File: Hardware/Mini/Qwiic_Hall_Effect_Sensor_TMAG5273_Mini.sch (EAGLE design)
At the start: 30 parts, among them J1 Vertical Qwiic Connector, J2 Vertical Qwiic Connector, Q1 20V/4.2A/52mΩ/1.4W, U1 TMAG5273

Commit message: Design Review Changes
Adjusted schematic to have the correct power-on reset circuit, along with the change in the layout. The GPIO net was relabled to RESET to match the layout of the board/labeling. Adjusted some labeling in the schematic.
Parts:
- removed R1: 330, SparkFun-Resistors:330OHM-0603-1/10W-1%
- removed R6: 10k, SparkFun-Resistors:10KOHM-0603-1/10W-1%
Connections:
- net INT renamed !INT
- removed net GPIO: J3.5, R6.1, R7.1
- removed net N$7: Q1.G, R6.2
- new net RESET: J3.5, Q1.G, R7.2
- net 3.3V: now also Q1.S; no longer R1.2, R7.2
- net 3.3V_SW: now also Q1.D; no longer Q1.S, R1.1
- net GND: now also R7.1; no longer Q1.D
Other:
- note added: "7-bit unshifted I2C Address: 0x35"
- note removed: "7-bit unshifted I2C Address: 0x35h"
- moved on the sheet: Q1, R7

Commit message: Adjusted from design review
Added truth tables, changed RESET to Disable, adjusted magnetic axis to be centered to the middle of the board, added push button for 1x1 reset option
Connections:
- net RESET renamed DISABLE
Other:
- note added: "Board Status"
- note added: "DISABLE Value"
- note added: "Disable to Header Reset"
- note added: "HIGH (3.3V)"
- note added: "LOW (0V) - default"
- note added: "Off"
- note added: "On"
- moved on the sheet: Q1, R7
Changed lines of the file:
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@@
 <wire x1="147.32" y1="35.56" x2="147.32" y2="114.3" width="0.2032" layer="97" style="longdash"/>
 <wire x1="195.58" y1="114.3" x2="195.58" y2="35.56" width="0.2032" layer="97" style="longdash"/>
+<wire x1="30.48" y1="121.92" x2="48.26" y2="121.92" width="0.2032" layer="97"/>
+<wire x1="48.26" y1="121.92" x2="60.96" y2="121.92" width="0.2032" layer="97"/>
+<wire x1="60.96" y1="121.92" x2="60.96" y2="129.54" width="0.2032" layer="97"/>
+<wire x1="60.96" y1="129.54" x2="48.26" y2="129.54" width="0.2032" layer="97"/>
+<wire x1="48.26" y1="129.54" x2="30.48" y2="129.54" width="0.2032" layer="97"/>
+<wire x1="48.26" y1="129.54" x2="48.26" y2="121.92" width="0.2032" layer="97"/>
+<text x="31.242" y="130.302" size="1.27" layer="97" font="vector">Disable to Header Reset</text>
+<wire x1="30.48" y1="129.54" x2="30.48" y2="121.92" width="0.2032" layer="97"/>
+<wire x1="30.48" y1="127" x2="60.96" y2="127" width="0.2032" layer="97"/>
+<wire x1="30.48" y1="124.46" x2="60.96" y2="124.46" width="0.2032" layer="97"/>
+<text x="33.02" y="127.508" size="1.27" layer="97" font="vector">DISABLE Value</text>
+<text x="30.988" y="124.968" size="1.27" layer="97" font="vector">HIGH (3.3V)</text>
+<text x="30.988" y="122.428" size="1.27" layer="97" font="vector">LOW (0V) - default</text>
+<text x="48.768" y="124.968" size="1.27" layer="97" font="vector">Off</text>
+<text x="48.768" y="122.428" size="1.27" layer="97" font="vector">On</text>
+<text x="49.276" y="127.508" size="1.27" layer="97" font="vector">Board Status</text>
 </plain>
 <instances>
@@
 <attribute name="VALUE" x="174.244" y="81.28" size="1.778" layer="96" font="vector" rot="R90" align="top-center"/>
 </instance>
-<instance part="SUPPLY8" gate="G$1" x="50.8" y="160.02" smashed="yes">
-<attribute name="VALUE" x="50.8" y="162.814" size="1.778" layer="96" font="vector" align="bottom-center"/>
-</instance>
-<instance part="Q1" gate="G$1" x="48.26" y="152.4" smashed="yes" rot="MR180">
-<attribute name="NAME" x="53.34" y="154.94" size="1.778" layer="95" font="vector" rot="MR180"/>
-<attribute name="VALUE" x="53.34" y="157.48" size="1.778" layer="96" font="vector" rot="MR180"/>
-</instance>
-<instance part="SUPPLY11" gate="G$1" x="58.42" y="144.78" smashed="yes">
-<attribute name="VALUE" x="58.42" y="147.574" size="1.778" layer="96" font="vector" align="bottom-center"/>
-</instance>
-<instance part="R7" gate="G$1" x="38.1" y="147.32" smashed="yes" rot="R90">
-<attribute name="NAME" x="36.576" y="147.32" size="1.778" layer="95" font="vector" rot="R90" align="bottom-center"/>
-<attribute name="VALUE" x="39.624" y="147.32" size="1.778" layer="96" font="vector" rot="R90" align="top-center"/>
-</instance>
-<instance part="GND7" gate="1" x="38.1" y="137.16" smashed="yes">
-<attribute name="VALUE" x="38.1" y="136.906" size="1.778" layer="96" font="vector" align="top-center"/>
+<instance part="SUPPLY8" gate="G$1" x="50.8" y="165.1" smashed="yes">
+<attribute name="VALUE" x="50.8" y="167.894" size="1.778" layer="96" font="vector" align="bottom-center"/>
+</instance>
+<instance part="Q1" gate="G$1" x="48.26" y="157.48" smashed="yes" rot="MR180">
+<attribute name="NAME" x="53.34" y="160.02" size="1.778" layer="95" font="vector" rot="MR180"/>
+<attribute name="VALUE" x="53.34" y="162.56" size="1.778" layer="96" font="vector" rot="MR180"/>
+</instance>
+<instance part="SUPPLY11" gate="G$1" x="58.42" y="149.86" smashed="yes">
+<attribute name="VALUE" x="58.42" y="152.654" size="1.778" layer="96" font="vector" align="bottom-center"/>
+</instance>
+<instance part="R7" gate="G$1" x="38.1" y="152.4" smashed="yes" rot="R90">
+<attribute name="NAME" x="36.576" y="152.4" size="1.778" layer="95" font="vector" rot="R90" align="bottom-center"/>
+<attribute name="VALUE" x="39.624" y="152.4" size="1.778" layer="96" font="vector" rot="R90" align="top-center"/>
+</instance>
+<instance part="GND7" gate="1" x="38.1" y="142.24" smashed="yes">
+<attribute name="VALUE" x="38.1" y="141.986" size="1.778" layer="96" font="vector" align="top-center"/>
 </instance>
 </instances>
@@
 <pinref part="Q1" gate="G$1" pin="S"/>
 <pinref part="SUPPLY8" gate="G$1" pin="3.3V"/>
-<wire x1="50.8" y1="157.48" x2="50.8" y2="160.02" width="0.1524" layer="91"/>
+<wire x1="50.8" y1="162.56" x2="50.8" y2="165.1" width="0.1524" layer="91"/>
 </segment>
 </net>
@@
 <pinref part="GND7" gate="1" pin="GND"/>
 <pinref part="R7" gate="G$1" pin="1"/>
-<wire x1="38.1" y1="139.7" x2="38.1" y2="142.24" width="0.1524" layer="91"/>
+<wire x1="38.1" y1="144.78" x2="38.1" y2="147.32" width="0.1524" layer="91"/>
 </segment>
 </net>
@@
 <segment>
 <pinref part="Q1" gate="G$1" pin="D"/>
-<wire x1="50.8" y1="147.32" x2="50.8" y2="142.24" width="0.1524" layer="91"/>
-<wire x1="50.8" y1="142.24" x2="58.42" y2="142.24" width="0.1524" layer="91"/>
+<wire x1="50.8" y1="152.4" x2="50.8" y2="147.32" width="0.1524" layer="91"/>
+<wire x1="50.8" y1="147.32" x2="58.42" y2="147.32" width="0.1524" layer="91"/>
 <pinref part="SUPPLY11" gate="G$1" pin="3.3V_SW"/>
-<wire x1="58.42" y1="142.24" x2="58.42" y2="144.78" width="0.1524" layer="91"/>
-</segment>
-</net>
-<net name="RESET" class="0">
-<segment>
-<wire x1="20.32" y1="76.2" x2="25.4" y2="76.2" width="0.1524" layer="91"/>
-<label x="25.4" y="76.2" size="1.27" layer="95" font="vector" xref="yes"/>
-<pinref part="J3" gate="J1" pin="5"/>
-</segment>
-<segment>
-<pinref part="Q1" gate="G$1" pin="G"/>
-<wire x1="43.18" y1="154.94" x2="38.1" y2="154.94" width="0.1524" layer="91"/>
-<pinref part="R7" gate="G$1" pin="2"/>
-<wire x1="38.1" y1="154.94" x2="33.02" y2="154.94" width="0.1524" layer="91"/>
-<wire x1="38.1" y1="152.4" x2="38.1" y2="154.94" width="0.1524" layer="91"/>
-<junction x="38.1" y="154.94"/>
-<label x="33.02" y="154.94" size="1.27" layer="95" font="vector" rot="R180" xref="yes"/>
+<wire x1="58.42" y1="147.32" x2="58.42" y2="149.86" width="0.1524" layer="91"/>
 </segment>
 </net>
@@
 </segment>
 </net>
+<net name="DISABLE" class="0">
+<segment>
+<pinref part="Q1" gate="G$1" pin="G"/>
+<wire x1="43.18" y1="160.02" x2="38.1" y2="160.02" width="0.1524" layer="91"/>
+<pinref part="R7" gate="G$1" pin="2"/>
+<wire x1="38.1" y1="160.02" x2="33.02" y2="160.02" width="0.1524" layer="91"/>
+<wire x1="38.1" y1="157.48" x2="38.1" y2="160.02" width="0.1524" layer="91"/>
+<junction x="38.1" y="160.02"/>
+<label x="33.02" y="160.02" size="1.27" layer="95" font="vector" rot="R180" xref="yes"/>
+</segment>
+<segment>
+<wire x1="20.32" y1="76.2" x2="25.4" y2="76.2" width="0.1524" layer="91"/>
+<label x="25.4" y="76.2" size="1.27" layer="95" font="vector" xref="yes"/>
+<pinref part="J3" gate="J1" pin="5"/>
+</segment>
+</net>

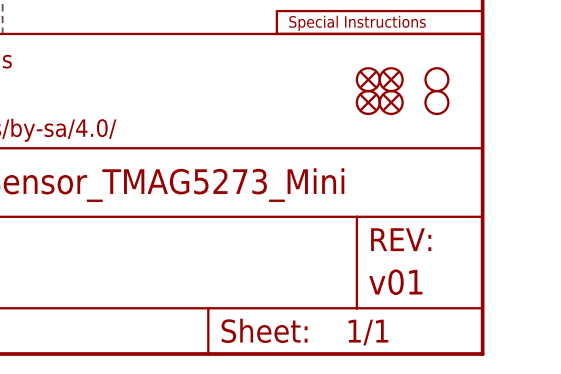
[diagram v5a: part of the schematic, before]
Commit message: Design review updates
Addition of gerber files for both mini and 1x1, adjusted board for reds engineering checklist run.
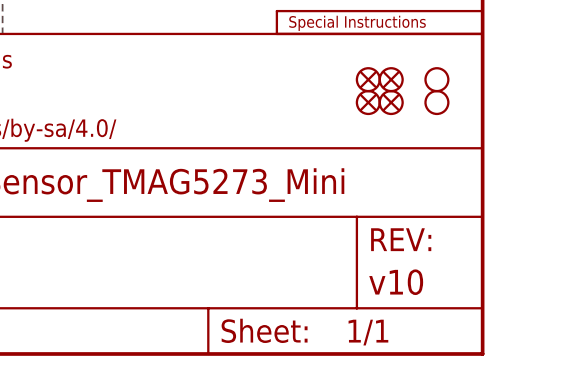
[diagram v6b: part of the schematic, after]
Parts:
- FRAME1: REV v01 -> v10
- LOGO6: value SFE_LOGO_FLAME0.05_INCH -> SFE_LOGO_FLAME.1_INCH; device SparkFun-Aesthetics:SFE_LOGO_FLAME0.05_INCH -> SparkFun-Aesthetics:SFE_LOGO_FLAME.1_INCH
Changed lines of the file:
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@@
 <part name="FRAME1" library="SparkFun-Aesthetics" deviceset="FRAME-LETTER" device="">
 <attribute name="DESIGNER" value="M. Chodikov"/>
-<attribute name="REV" value="v01"/>
+<attribute name="REV" value="v10"/>
 </part>
 <part name="U1" library="TMAG5273" deviceset="TMAG5273A1QDBVT" device="" value="TMAG5273"/>
@@
 <part name="LOGO3" library="SparkFun-Aesthetics" deviceset="QWIIC_LOGO" device="_4MM" value="QWIIC_LOGO_4MM"/>
 <part name="LOGO2" library="SparkFun-Aesthetics" deviceset="SFE_LOGO_NAME_FLAME" device="5_MM" value="SFE_LOGO_NAME_FLAME5_MM"/>
-<part name="LOGO6" library="SparkFun-Aesthetics" deviceset="SFE_LOGO_FLAME" device="0.05_INCH" value="SFE_LOGO_FLAME0.05_INCH"/>
+<part name="LOGO6" library="SparkFun-Aesthetics" deviceset="SFE_LOGO_FLAME" device=".1_INCH" value="SFE_LOGO_FLAME.1_INCH"/>
 <part name="LOGO4" library="SparkFun-Aesthetics" deviceset="SFE_LOGO_NAME" device="7_MM" value="SFE_LOGO_NAME7_MM"/>
 <part name="FD1" library="SparkFun-Aesthetics" deviceset="FIDUCIAL" device="1X2"/>

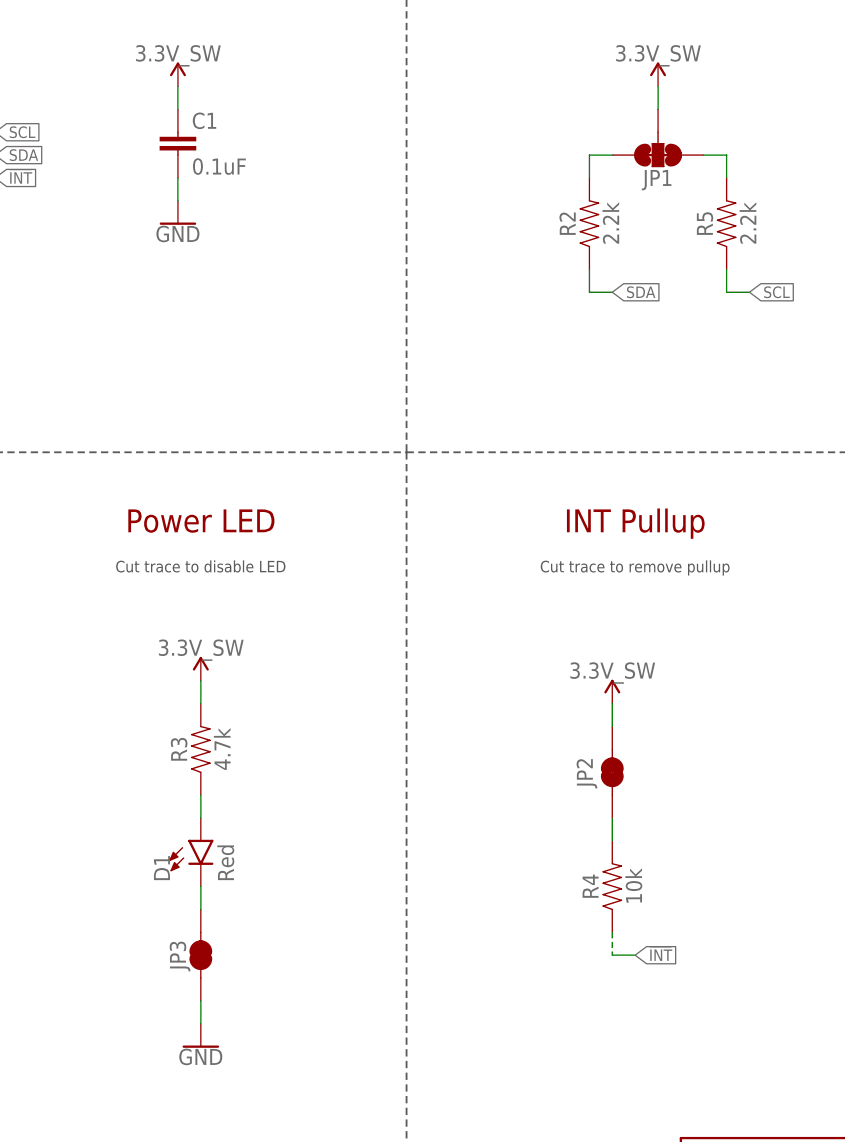
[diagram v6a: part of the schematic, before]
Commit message: Updates from design review
Adjusted traces for better GND connections; changed direction of tail end for the DISABLE pin; changed jumper names in schematic to match layout; added more GND vias to the Mini; updated trace widths to be the correct size
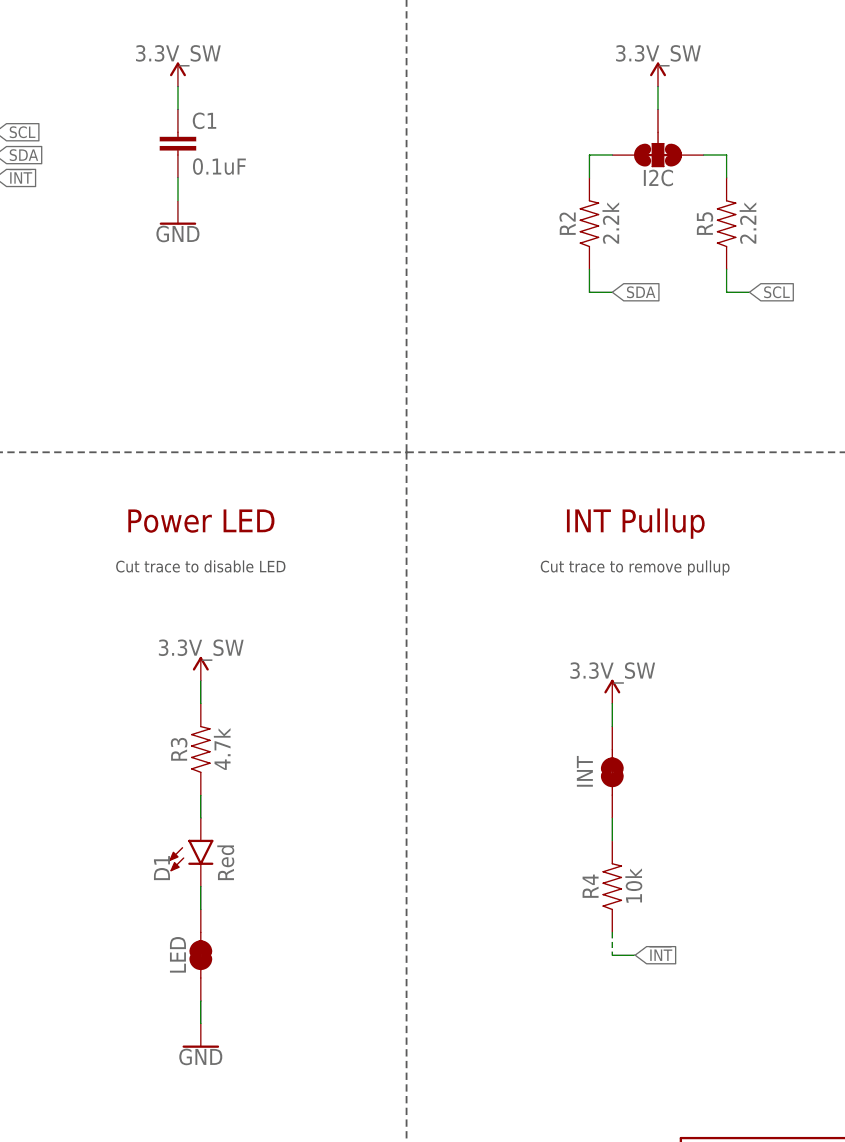
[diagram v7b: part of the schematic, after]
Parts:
- renumbered JP1 to I2C, JP2 to INT, JP3 to LED
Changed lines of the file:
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@@
 <part name="GND4" library="SparkFun-PowerSymbols" deviceset="GND" device=""/>
 <part name="GND5" library="SparkFun-PowerSymbols" deviceset="GND" device=""/>
-<part name="JP3" library="SparkFun-Jumpers" deviceset="JUMPER-SMT_2_NC_TRACE" device="_SILK" package3d_urn="urn:adsk.eagle:package:39281/1"/>
-<part name="JP2" library="SparkFun-Jumpers" deviceset="JUMPER-SMT_2_NC_TRACE" device="_SILK" package3d_urn="urn:adsk.eagle:package:39281/1"/>
+<part name="LED" library="SparkFun-Jumpers" deviceset="JUMPER-SMT_2_NC_TRACE" device="_SILK" package3d_urn="urn:adsk.eagle:package:39281/1"/>
+<part name="INT" library="SparkFun-Jumpers" deviceset="JUMPER-SMT_2_NC_TRACE" device="_SILK" package3d_urn="urn:adsk.eagle:package:39281/1"/>
 <part name="R4" library="SparkFun-Resistors" deviceset="10KOHM" device="-0603-1/10W-1%" value="10k"/>
 <part name="R2" library="SparkFun-Resistors" deviceset="2.2KOHM" device="-0603-1/10W-1%" value="2.2k"/>
 <part name="R5" library="SparkFun-Resistors" deviceset="2.2KOHM" device="-0603-1/10W-1%" value="2.2k"/>
-<part name="JP1" library="SparkFun-Jumpers" deviceset="JUMPER-SMT_3_2-NC_TRACE" device="_SILK" package3d_urn="urn:adsk.eagle:package:39289/1"/>
+<part name="I2C" library="SparkFun-Jumpers" deviceset="JUMPER-SMT_3_2-NC_TRACE" device="_SILK" package3d_urn="urn:adsk.eagle:package:39289/1"/>
 <part name="GND6" library="SparkFun-PowerSymbols" deviceset="GND" device=""/>
 <part name="SUPPLY9" library="SparkFun-PowerSymbols" deviceset="3.3V" device=""/>
@@
 <attribute name="VALUE" x="172.72" y="48.006" size="1.778" layer="96" font="vector" align="top-center"/>
 </instance>
-<instance part="JP3" gate="G$1" x="172.72" y="58.42" smashed="yes" rot="R90">
+<instance part="LED" gate="G$1" x="172.72" y="58.42" smashed="yes" rot="R90">
 <attribute name="NAME" x="170.18" y="58.42" size="1.778" layer="95" font="vector" rot="R90" align="center"/>
 <attribute name="VALUE" x="175.26" y="55.88" size="1.778" layer="96" font="vector" rot="R90" align="top-left" display="off"/>
 </instance>
-<instance part="JP2" gate="G$1" x="218.44" y="78.74" smashed="yes" rot="R90">
+<instance part="INT" gate="G$1" x="218.44" y="78.74" smashed="yes" rot="R90">
 <attribute name="NAME" x="215.392" y="78.74" size="1.778" layer="95" font="vector" rot="R90" align="center"/>
 <attribute name="VALUE" x="221.488" y="78.74" size="1.778" layer="96" font="vector" rot="R90" align="center" display="off"/>
@@
 <attribute name="VALUE" x="232.664" y="139.7" size="1.778" layer="96" font="vector" rot="R90" align="top-center"/>
 </instance>
-<instance part="JP1" gate="G$1" x="223.52" y="147.32" smashed="yes" rot="R270">
+<instance part="I2C" gate="G$1" x="223.52" y="147.32" smashed="yes" rot="R270">
 <attribute name="NAME" x="223.52" y="144.78" size="1.778" layer="95" font="vector" rot="R180" align="center"/>
 <attribute name="VALUE" x="243.459" y="149.86" size="1.778" layer="96" font="vector" rot="R270" align="top-center" display="off"/>
@@
 <segment>
 <pinref part="GND5" gate="1" pin="GND"/>
-<pinref part="JP3" gate="G$1" pin="1"/>
+<pinref part="LED" gate="G$1" pin="1"/>
 <wire x1="172.72" y1="50.8" x2="172.72" y2="53.34" width="0.1524" layer="91"/>
 </segment>
@@
 <net name="N$1" class="0">
 <segment>
-<pinref part="JP3" gate="G$1" pin="2"/>
+<pinref part="LED" gate="G$1" pin="2"/>
 <wire x1="172.72" y1="63.5" x2="172.72" y2="66.04" width="0.1524" layer="91"/>
 <pinref part="D1" gate="G$1" pin="C"/>
@@
 <net name="N$5" class="0">
 <segment>
-<pinref part="JP2" gate="G$1" pin="1"/>
+<pinref part="INT" gate="G$1" pin="1"/>
 <wire x1="218.44" y1="73.66" x2="218.44" y2="71.12" width="0.1524" layer="91"/>
 <pinref part="R4" gate="G$1" pin="2"/>
@@
 <wire x1="215.9" y1="144.78" x2="215.9" y2="147.32" width="0.1524" layer="91"/>
 <wire x1="215.9" y1="147.32" x2="218.44" y2="147.32" width="0.1524" layer="91"/>
-<pinref part="JP1" gate="G$1" pin="3"/>
+<pinref part="I2C" gate="G$1" pin="3"/>
 </segment>
 </net>
@@
 <wire x1="228.6" y1="147.32" x2="231.14" y2="147.32" width="0.1524" layer="91"/>
 <wire x1="231.14" y1="147.32" x2="231.14" y2="144.78" width="0.1524" layer="91"/>
-<pinref part="JP1" gate="G$1" pin="1"/>
+<pinref part="I2C" gate="G$1" pin="1"/>
 </segment>
 </net>
@@
 <segment>
 <wire x1="223.52" y1="152.4" x2="223.52" y2="154.94" width="0.1524" layer="91"/>
-<pinref part="JP1" gate="G$1" pin="2"/>
+<pinref part="I2C" gate="G$1" pin="2"/>
 <pinref part="SUPPLY4" gate="G$1" pin="3.3V_SW"/>
 </segment>
@@
 <segment>
 <wire x1="218.44" y1="83.82" x2="218.44" y2="86.36" width="0.1524" layer="91"/>
-<pinref part="JP2" gate="G$1" pin="2"/>
+<pinref part="INT" gate="G$1" pin="2"/>
 <pinref part="SUPPLY7" gate="G$1" pin="3.3V_SW"/>
 </segment>

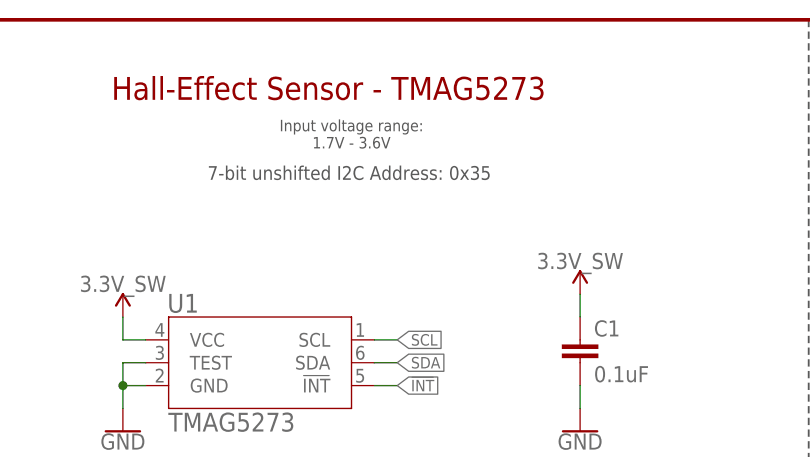
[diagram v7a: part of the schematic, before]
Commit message: Updated I2C address in schematic
Updated the I2C address to the actual address used in the library/for the devices usage
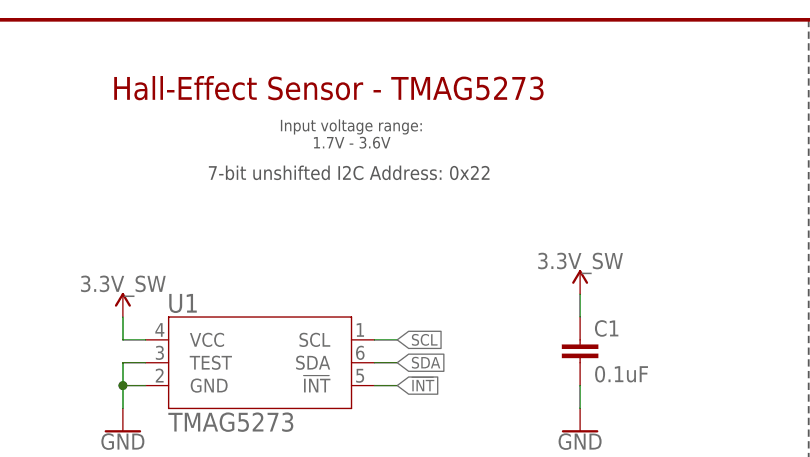
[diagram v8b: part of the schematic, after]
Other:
- note added: "7-bit unshifted I2C Address: 0x22"
- note removed: "7-bit unshifted I2C Address: 0x35"
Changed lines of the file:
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@@
 <sheet>
 <plain>
-<text x="128.778" y="167.64" size="1.524" layer="97" font="vector">7-bit unshifted I2C Address: 0x35</text>
+<text x="128.778" y="167.64" size="1.524" layer="97" font="vector">7-bit unshifted I2C Address: 0x22</text>
 <text x="142.24" y="177.8" size="2.54" layer="94" font="vector" align="center">Hall-Effect Sensor - TMAG5273</text>
 <text x="223.52" y="177.8" size="2.54" layer="94" font="vector" align="center">I²C Pullup</text>
